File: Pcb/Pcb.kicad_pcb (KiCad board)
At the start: 2 copper layers, 152.3 x 104.7 mm, 127 parts, among them J1 TRRS, Q1 2N7002, SW1 SW_Push, SW10 SW_Push, SW11 SW_Push, SW12 SW_Push, SW13 SW_Push, SW14 SW_Push, SW15 SW_Push, SW16 SW_Push, SW17 SW_Push, SW18 SW_Push, SW19 SW_Push, SW2 SW2, SW20 SW_Push, SW21 SW_Push, SW22 SW_Push, SW23 SW_Push, SW24 SW_Push, SW25 SW_Push, SW26 SW_Push, SW27 SW_Push, SW28 SW_Push, SW29 SW_Push, SW3 SW_Push, SW4 SW_Push, SW5 SW_Push, SW6 SW_Push, SW7 SW_Push, SW8 SW_Push, SW9 SW_Push, U1 ProMicro

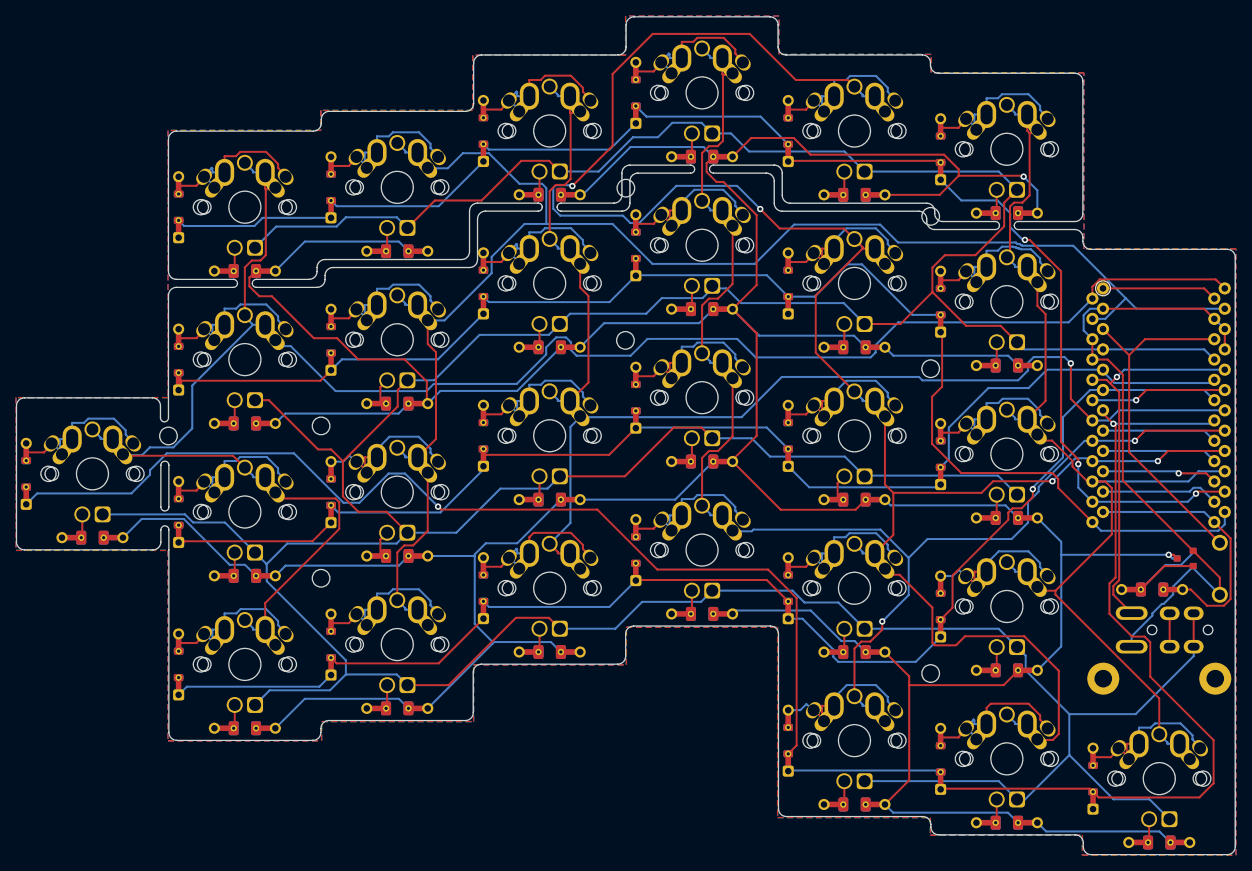
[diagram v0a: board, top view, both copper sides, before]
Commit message: Delete all tracks
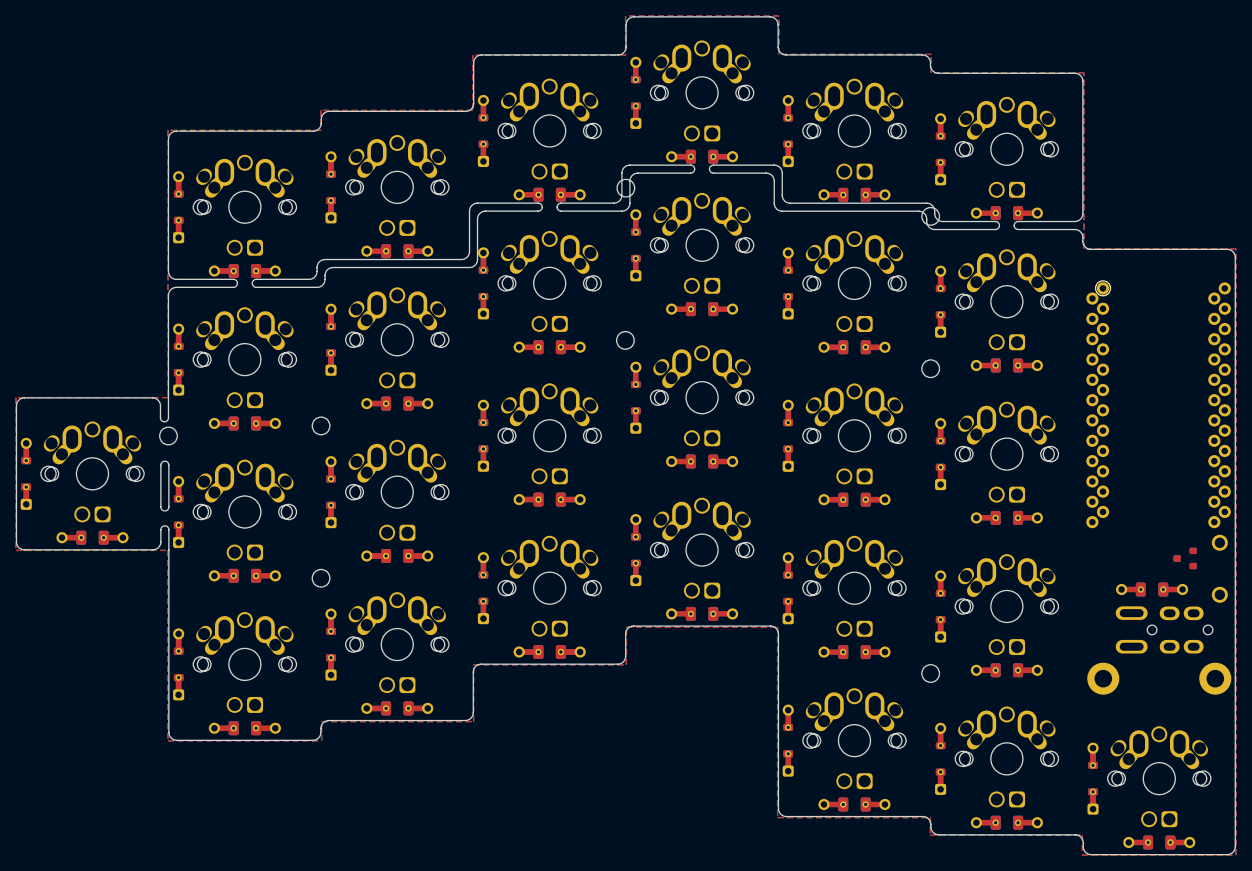
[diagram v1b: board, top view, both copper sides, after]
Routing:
- net /LEDOut: track 623.9 -> 0.00 mm, vias 2 -> 0
- net VCC: track 618.2 -> 0.00 mm
- net /rowE: track 259.5 -> 0.00 mm, vias 2 -> 0
- net /col4: track 253.2 -> 0.00 mm, vias 4 -> 0
- net /col0: track 250.3 -> 0.00 mm
- net /col1: track 200.2 -> 0.00 mm
- net /rowA: track 183.6 -> 0.00 mm, vias 3 -> 0
- net /rowB: track 176.9 -> 0.00 mm
- net /col3: track 174.8 -> 0.00 mm, vias 2 -> 0
- net /rowD: track 171.8 -> 0.00 mm, vias 1 -> 0
- net /col2: track 167.7 -> 0.00 mm, vias 1 -> 0
- net /rowC: track 158.8 -> 0.00 mm
- net /col5: track 135.8 -> 0.00 mm
- net GND: track 82.9 -> 0.00 mm
- net /SDA: track 47.9 -> 0.00 mm, vias 1 -> 0
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
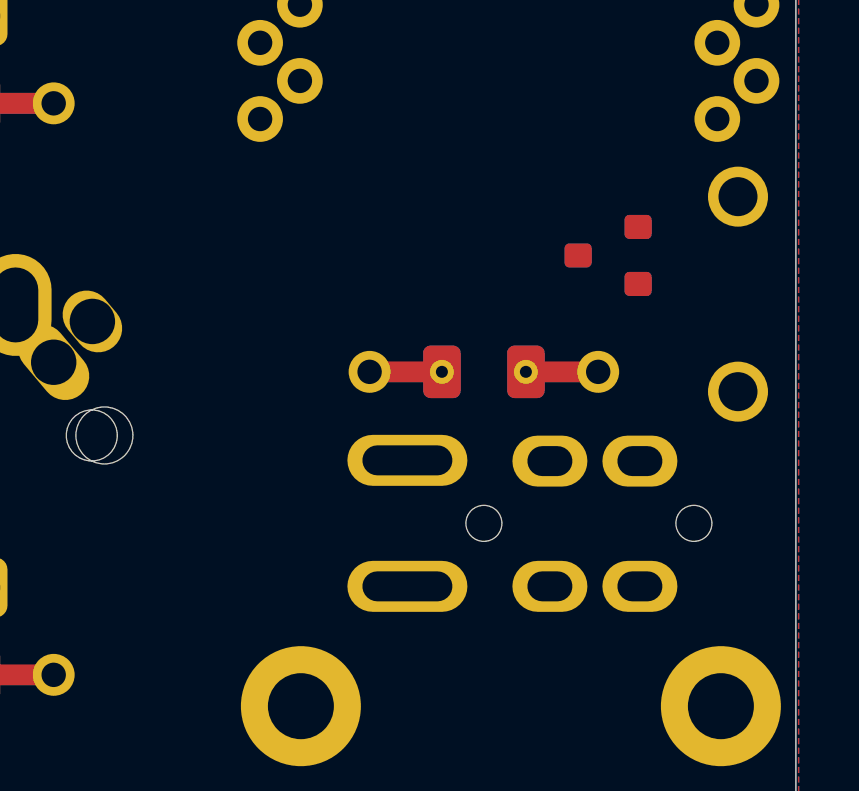
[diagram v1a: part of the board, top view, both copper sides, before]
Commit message: Placed resistors and jumpers
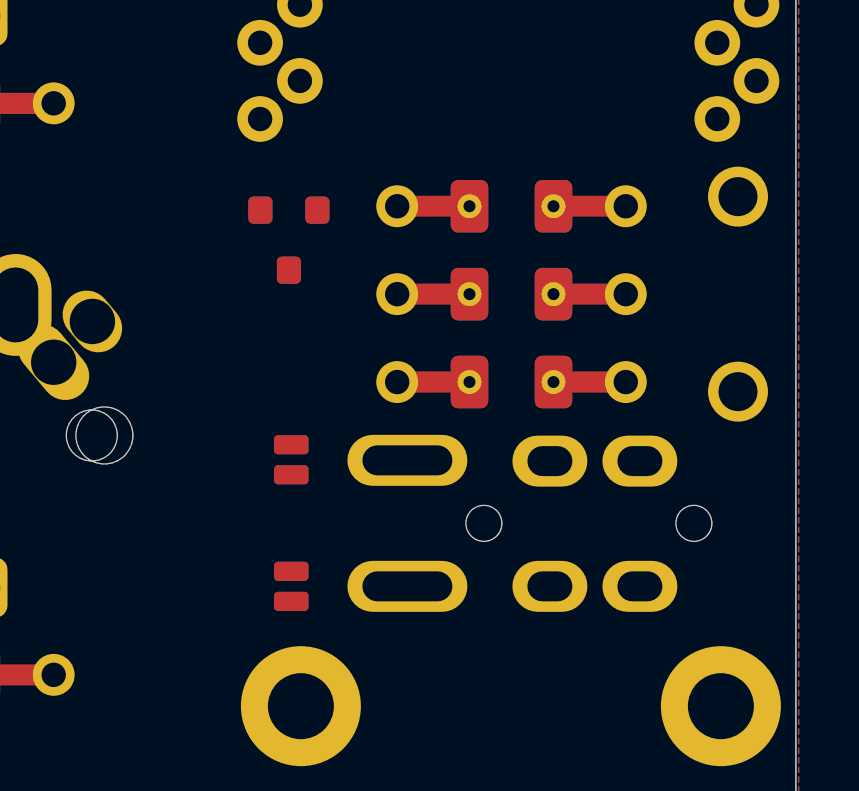
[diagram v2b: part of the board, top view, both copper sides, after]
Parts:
- added JP1: Jumper, Used_Footprints:Jumper_SMD, B.Cu at (212.7, 104.6)
- added JP2: Jumper, Used_Footprints:Jumper_SMD, F.Cu at (212.7, 104.6)
- added JP3: Jumper, Used_Footprints:Jumper_SMD, F.Cu at (212.7, 108.8)
- added JP4: Jumper, Used_Footprints:Jumper_SMD, B.Cu at (212.7, 108.8)
- added R29: 4.7K, Used_Footprints:Resistor_Hybrid_1205, F.Cu at (220.0, 102.0)
- added R30: 4.7K, Used_Footprints:Resistor_Hybrid_1205, F.Cu at (220.0, 99.1)
- D1, D10, D11, D12, D13, D14, D15, D16, D17, D18, D19, D2, D20, D21, D22, D23, D24, D25, D26, D27, D28, D3, D4, D5, D6, D7, D8, D9: value D_Small -> 1N4148
- R1, R10, R11, R12, R13, R14, R15, R16, R17, R18, R19, R2, R20, R21, R22, R23, R24, R25, R26, R27, R28, R3, R4, R5, R6, R7, R8, R9: value R_Small -> 300R
- moved Q1 10.6 mm to (212.7, 97.2), turned to 270 degrees
- moved R31 5.60 mm to (220.0, 96.2)
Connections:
- net RST renamed /RST
- J1 pad A: /SDA -> Net-(J1-PadA)
- J1 pad B: VCC -> GND
- J1 pad C: Net-(J1-PadC) -> VCC
- J1 pad D: GND -> Net-(J1-PadD)
- U1 pad 5: /SDA -> SDA
- U1 pad 6: Net-(U1-Pad6) -> SCL

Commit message: Add logo
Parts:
- added LG***: Silk_Logo_New, Used_Footprints:Silk_Logo_New, B.Cu at (219.9, 77.2)
- added LG***: Silk_Logo_New, Used_Footprints:Silk_Logo_New, F.Cu at (219.9, 77.2)

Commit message: Route tracks
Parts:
- renumbered LG*** to LG1, LG*** to LG2
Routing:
- net VCC: track 0.00 -> 629.7 mm, vias 0 -> 1
- net /LEDOut: track 0.00 -> 587.6 mm
- net /rowE: track 0.00 -> 262.4 mm, vias 0 -> 1
- net /col0: track 0.00 -> 231.9 mm
- net /col1: track 0.00 -> 199.0 mm, vias 0 -> 1
- net /rowA: track 0.00 -> 197.9 mm, vias 0 -> 3
- net /col3: track 0.00 -> 196.4 mm, vias 0 -> 2
- net /rowD: track 0.00 -> 191.5 mm
- net /col4: track 0.00 -> 176.9 mm
- net /rowB: track 0.00 -> 176.6 mm, vias 0 -> 1
- net /col2: track 0.00 -> 162.4 mm
- net /rowC: track 0.00 -> 156.7 mm, vias 0 -> 1
- net /col5: track 0.00 -> 134.3 mm
- net GND: track 0.00 -> 80.5 mm, vias 0 -> 1
- net SDA: track 0.00 -> 65.0 mm, vias 0 -> 1
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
